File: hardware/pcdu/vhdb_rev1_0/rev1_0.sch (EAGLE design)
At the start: 32 parts, among them SW1 KSZ9897RTXC

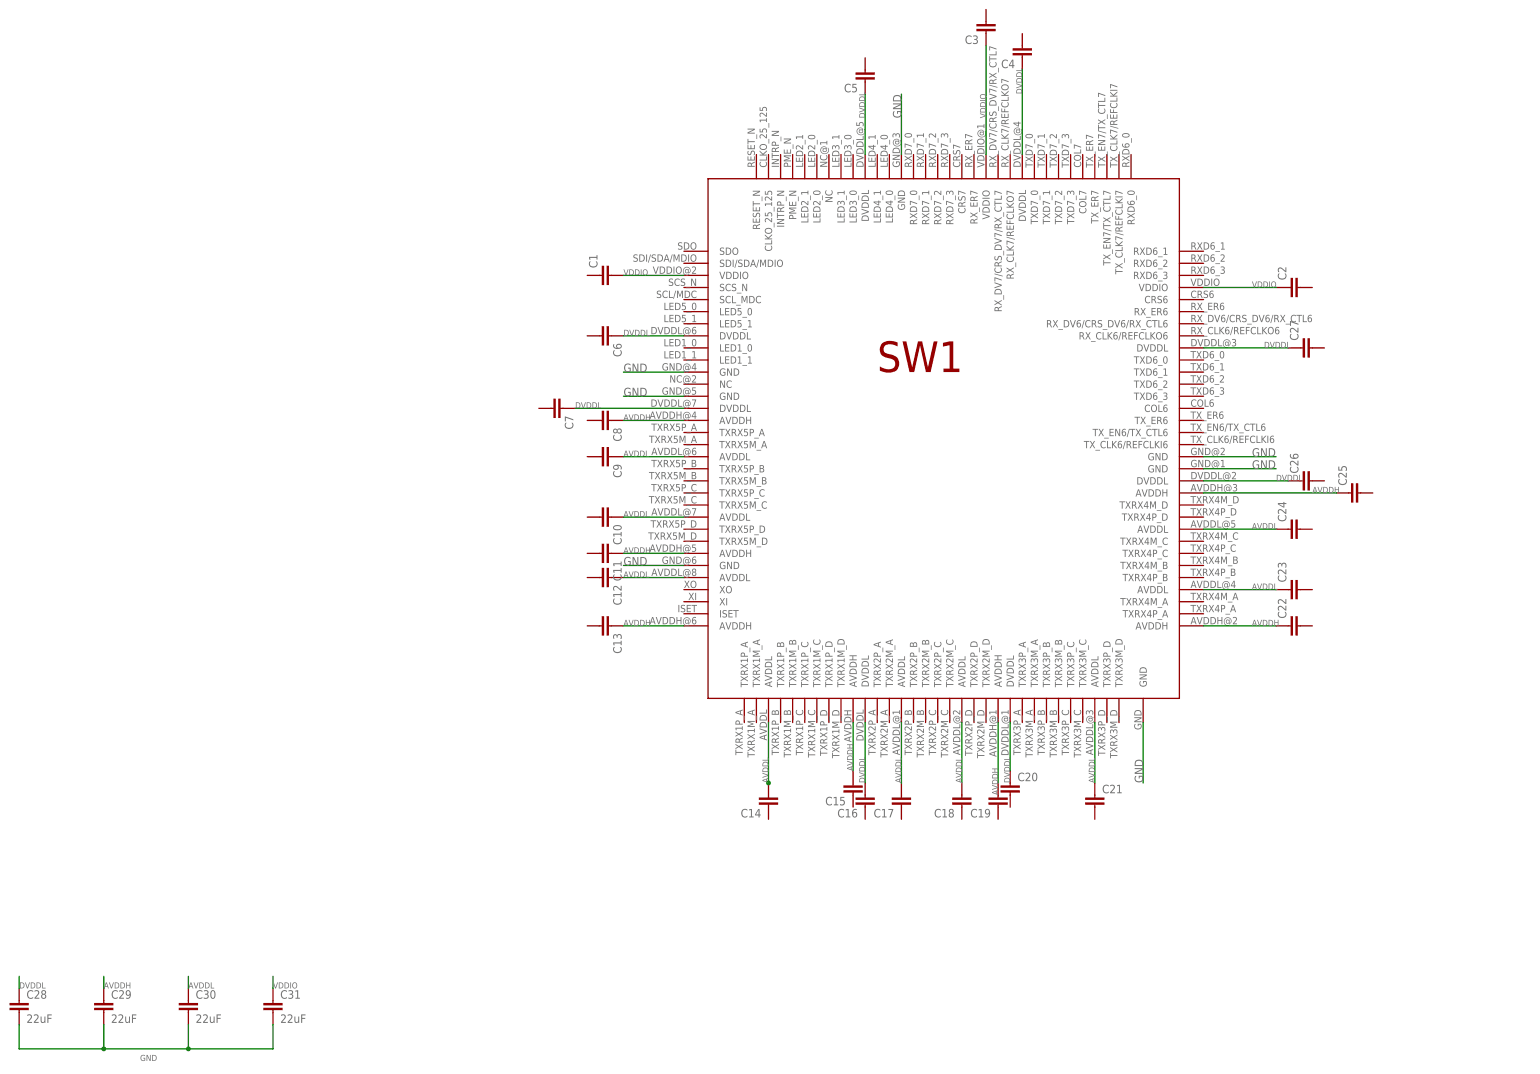
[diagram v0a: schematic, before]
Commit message: Restructured Switch IC symbol, added male rj45 connector library
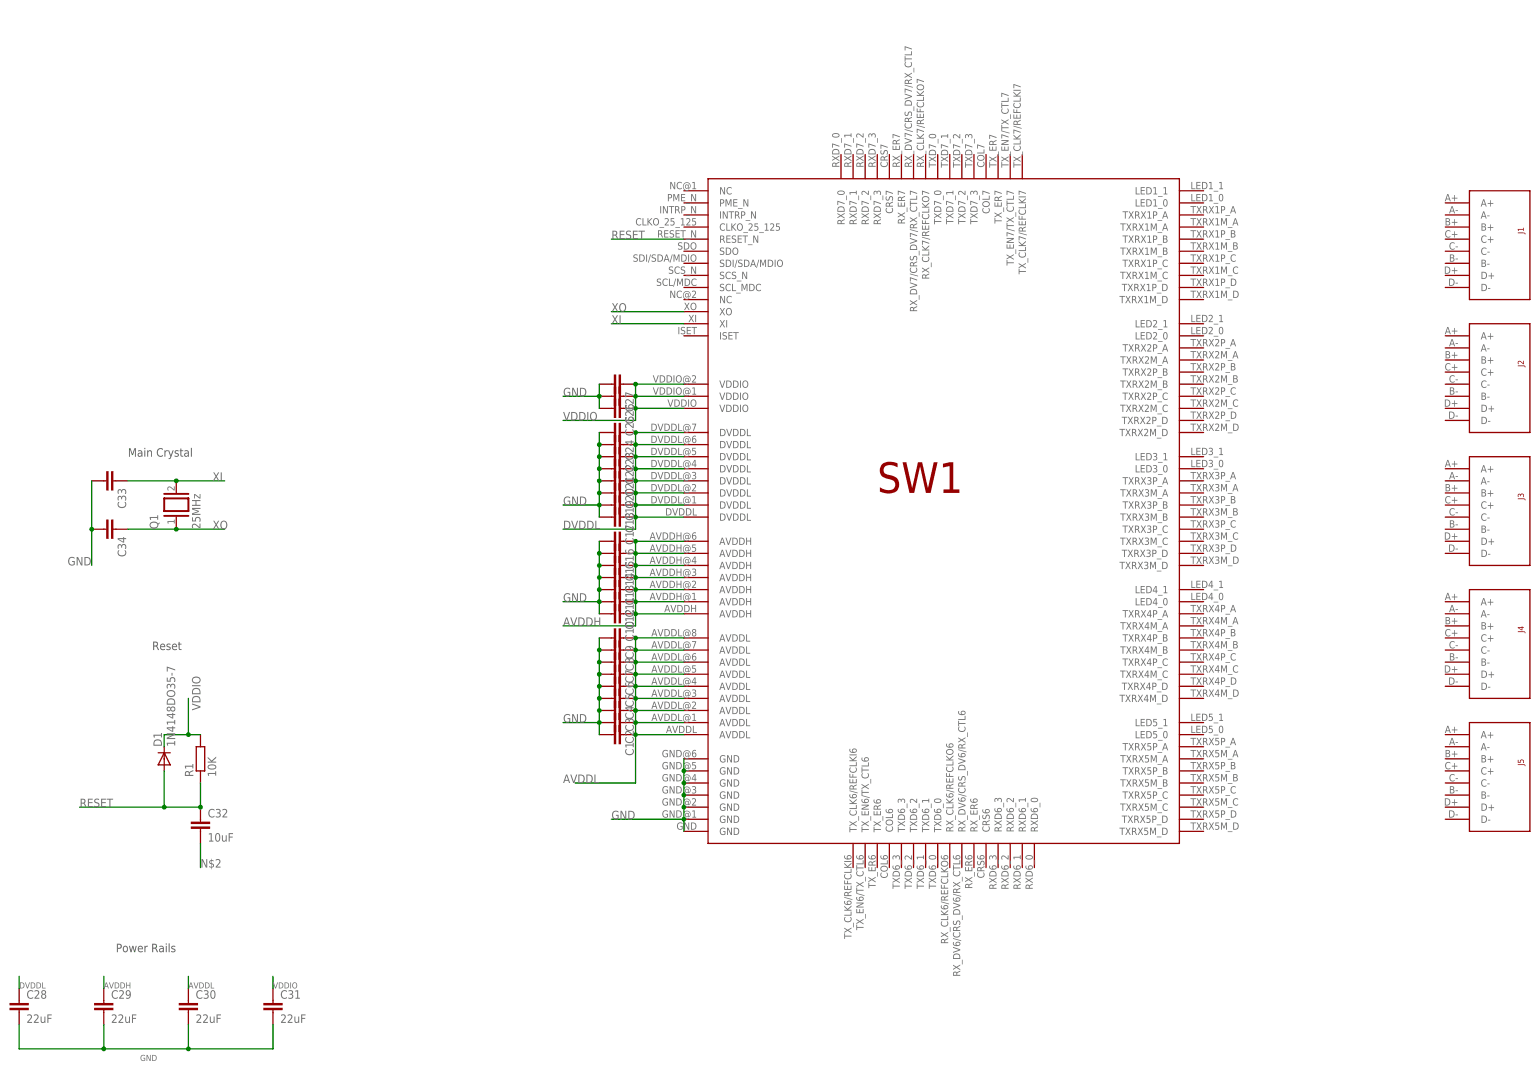
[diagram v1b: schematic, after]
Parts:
- added C32: 10uF, resistor:C-EUC0805
- added C33, C34: (no value), rcl:C-EUC0805
- added D1: 1N4148DO35-7, diode:1N4148DO35-7
- added J1, J2, J3, J4, J5: AJP92A8813, AJP92A8813:AJP92A8813
- added Q1: 25MHz, special:XTAL/S
- added R1: 10K, resistor:R-EU_R0805
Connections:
- new net N$2: C32.2
- new net RESET: C32.1, D1.A, R1.1, SW1.RESET_N
- new net XI: C33.1, Q1.2, SW1.XI
- new net XO: C34.1, Q1.1, SW1.XO
- net AVDDH: now also C10.1, C12.1, C14.1, C15.1, C16.1; no longer C15.2, C19.2, C22.1, C25.1, C8.1
- net AVDDL: now also C1.1, C2.1, C3.1, C4.1, C5.1, C6.1, C7.1, C8.1; no longer C10.1, C12.1, C14.2, C17.2, C18.2, C21.1, C23.1, C24.1
- net DVDDL: now also C17.1, C24.1, SW1.DVDDL@5; no longer C16.2, C20.1, C26.1, C27.1, C4.1, C5.1, C6.1, C7.1
- net GND: now also C1.2, C10.2, C11.2, C12.2, C13.2, C14.2, C15.2, C16.2, C17.2, C18.2, C19.2, C2.2, C20.2, C21.2, C22.2, C23.2, C24.2, C25.2, C26.2, C27.2, C3.2, C33.2, C34.2, C4.2, C5.2, C6.2, C7.2, C8.2, C9.2
- net VDDIO: now also C25.1, C26.1, C27.1, D1.C, R1.2; no longer C1.2, C2.1, C3.1
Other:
- note added: "Main Crystal"
- note added: "Power Rails"
- note added: "Reset"
- moved on the sheet: C1, C10, C11, C12, C13, C14, C15, C16, C17, C18, C19, C2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

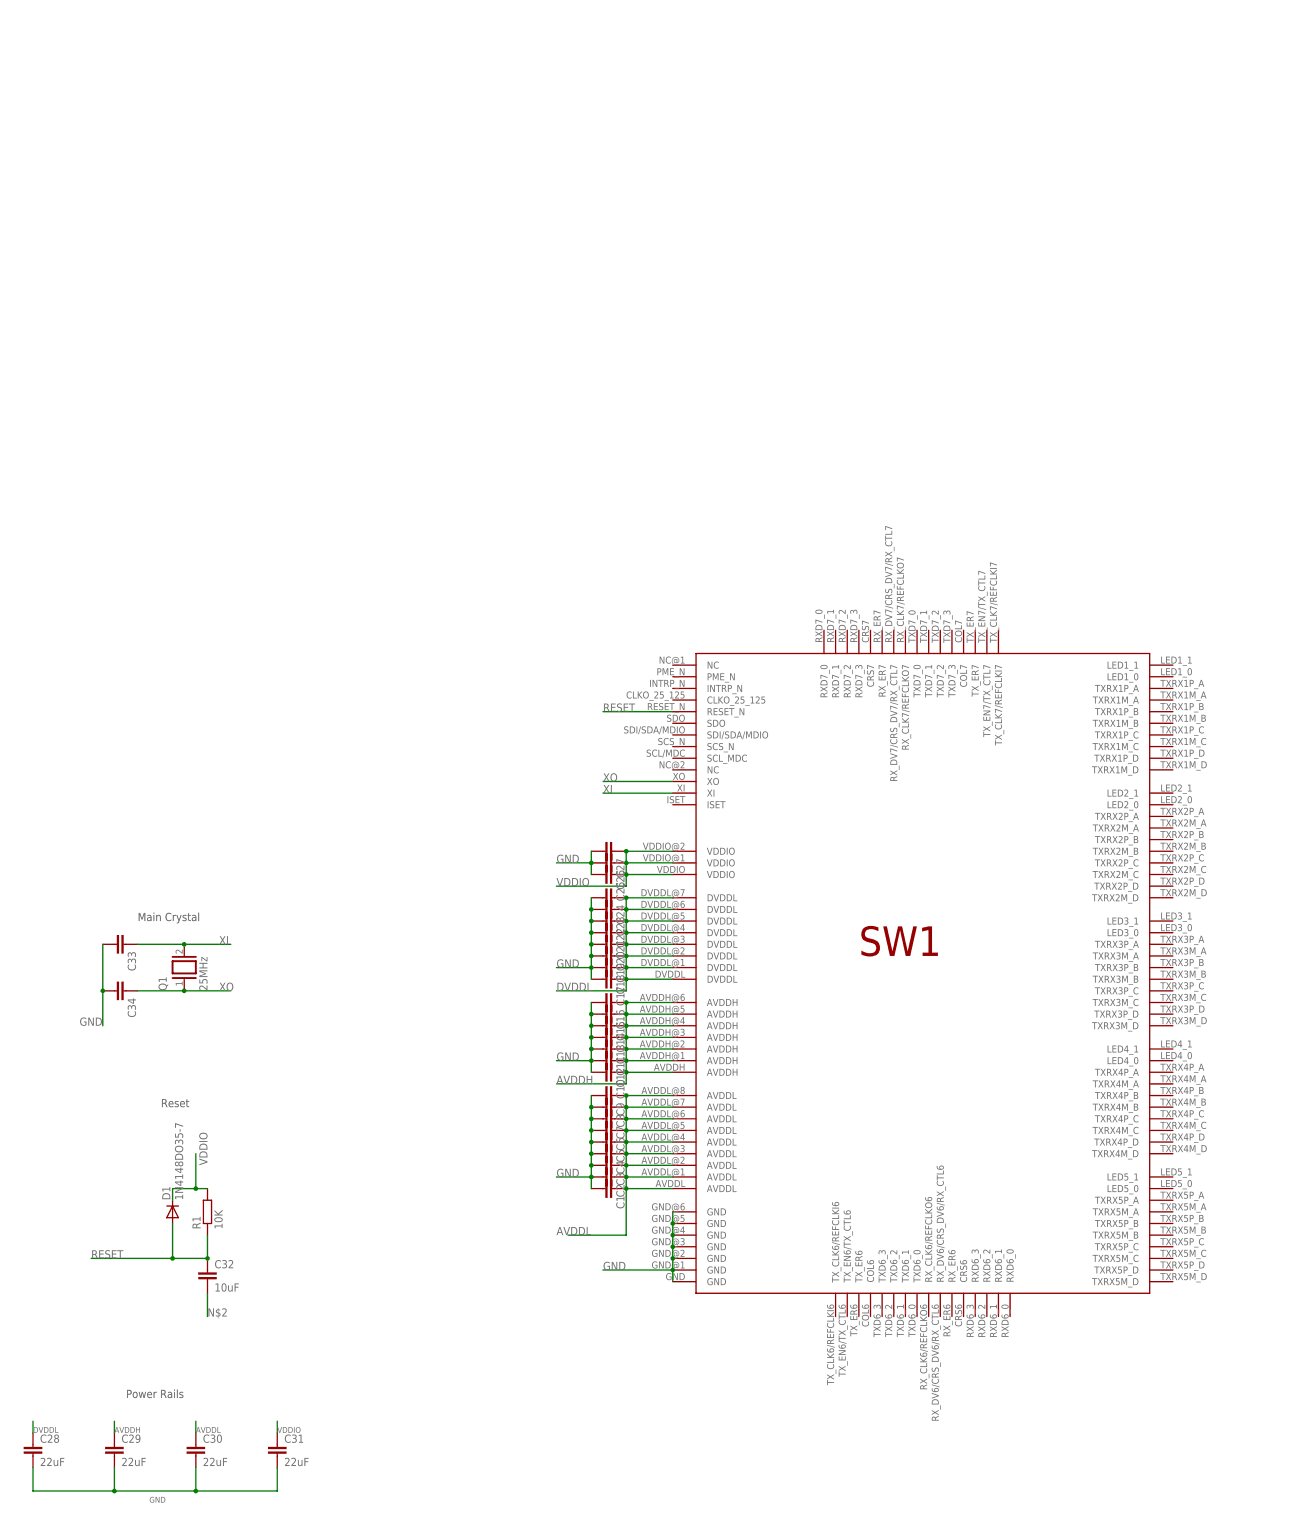
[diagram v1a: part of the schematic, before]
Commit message: Added PHY to vhdb uplink
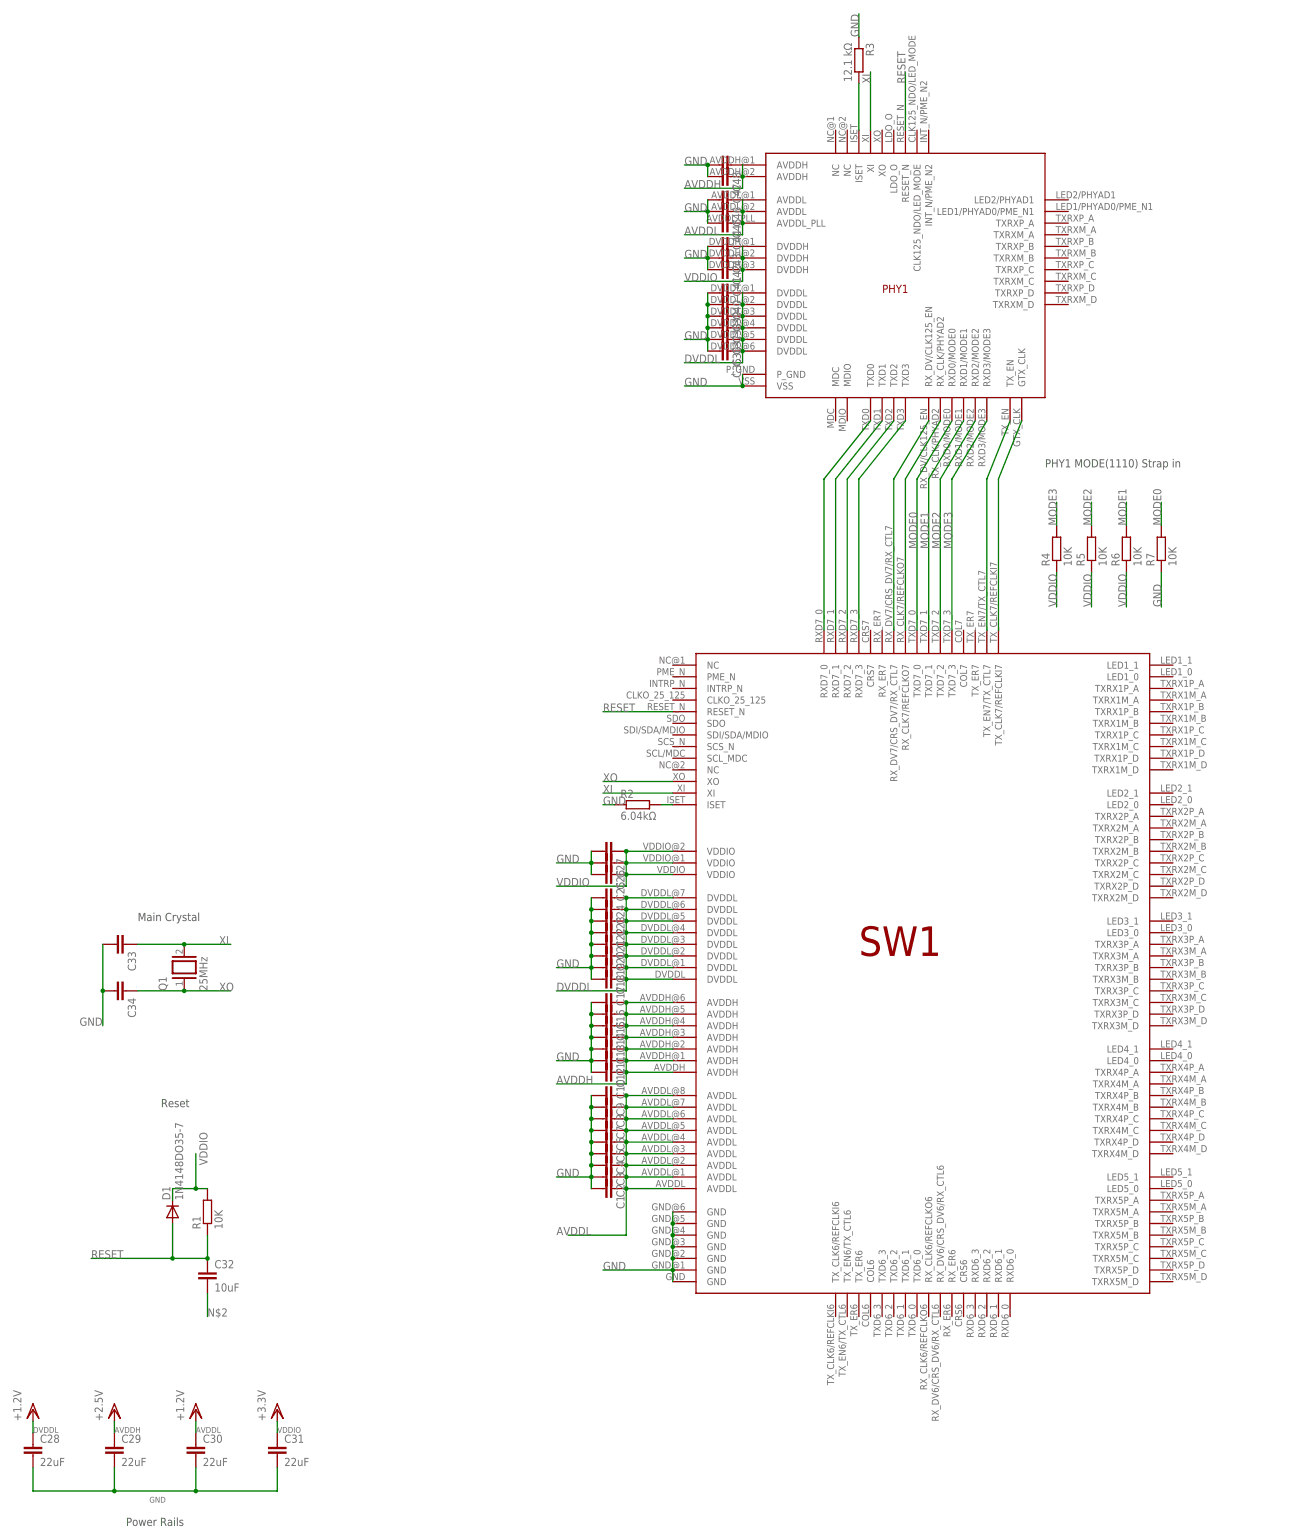
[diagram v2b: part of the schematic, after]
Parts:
- added C35, C36, C37, C38, C39, C40, C41, C42, C43, C44, C45, C46, C47, C48: (no value), rcl:C-EUC0805
- added PHY1: KSZ9031RNX, KSZ9031RNX:KSZ9031RNX
- added R2: 6.04kΩ, resistor:R-EU_R0805
- added R3: 12.1 kΩ, resistor:R-EU_R0805
- added R4, R5, R6, R7: 10K, resistor:R-EU_R0805
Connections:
- new net MODE0: PHY1.RXD0/MODE0, R7.2, SW1.TXD7_0
- new net MODE1: PHY1.RXD1/MODE1, R6.2
- new net MODE2: PHY1.RXD2/MODE2, R5.2
- new net MODE3: PHY1.RXD3/MODE3, R4.2, SW1.TXD7_3
- new net N$10: PHY1.TX_EN, SW1.TX_EN7/TX_CTL7
- new net N$11: PHY1.GTX_CLK, SW1.TX_CLK7/REFCLKI7
- new net N$12: PHY1.RX_DV/CLK125_EN, SW1.RX_DV7/CRS_DV7/RX_CTL7
- new net N$13: PHY1.RX_CLK/PHYAD2, SW1.RX_CLK7/REFCLKO7
- new net N$14: R2.2, SW1.ISET
- new net N$15: PHY1.ISET, R3.2
- new net N$6: PHY1.TXD0, SW1.RXD7_0
- new net N$7: PHY1.TXD1, SW1.RXD7_1
- new net N$8: PHY1.TXD2, SW1.RXD7_2
- new net N$9: PHY1.TXD3, SW1.RXD7_3
- net AVDDH: now also PHY1.AVDDH@1, PHY1.AVDDH@2
- net AVDDL: now also PHY1.AVDDL@1, PHY1.AVDDL@2, PHY1.AVDDL_PLL
- net DVDDL: now also C35.1, PHY1.DVDDL@1, PHY1.DVDDL@2, PHY1.DVDDL@3, PHY1.DVDDL@4, PHY1.DVDDL@5, PHY1.DVDDL@6
- net GND: now also C35.2, C37.2, C38.2, C39.2, C40.2, C41.2, C43.2, C44.2, C46.2, C47.2, C48.2, PHY1.P_GND, PHY1.VSS, R2.1, R3.1, R7.1
- net RESET: now also PHY1.RESET_N
- net VDDIO: now also PHY1.DVDDH@1, PHY1.DVDDH@2, PHY1.DVDDH@3, R4.1, R5.1, R6.1
- net XI: now also PHY1.XI
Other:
- note added: "PHY1 MODE(1110) Strap in"
